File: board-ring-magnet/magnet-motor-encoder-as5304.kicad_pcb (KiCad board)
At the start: 2 copper layers, 38.7 x 12.7 mm, 11 parts, among them U1 DS18B20, U2 AS5304

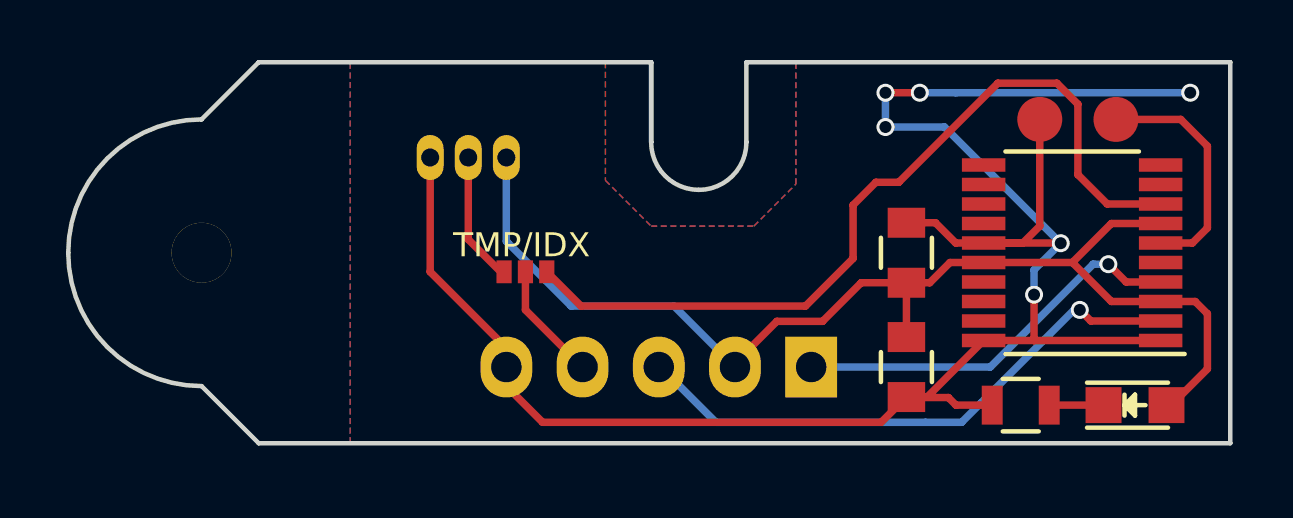
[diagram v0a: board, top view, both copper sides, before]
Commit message: board as5304: finish pcb layout and silkscreen
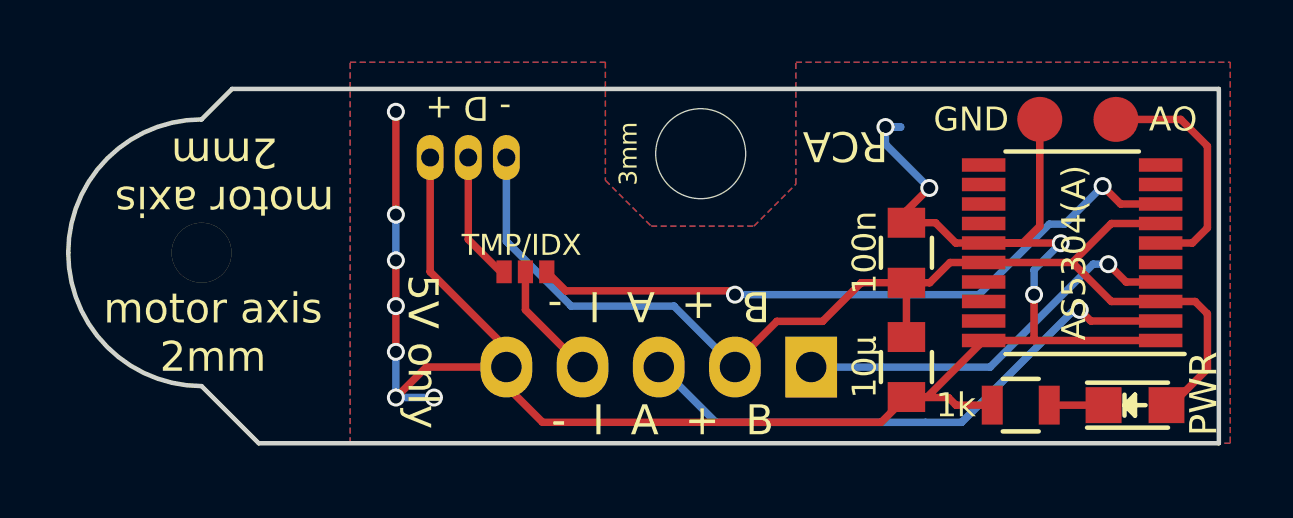
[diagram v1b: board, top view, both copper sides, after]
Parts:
- added REF**: 3mm, Mounting_Holes:MountingHole_3mm, F.Cu at (90.3, 43.7)
- U2: value AS5304 -> AS5304(A)
- renumbered GND to W1, AO to W2
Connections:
- net Net-(JP1-Pad1) renamed /B
- net Net-(JP1-Pad3) renamed /A
- net Net-(JP1-Pad4) renamed /TMP_IDX
- net Net-(SJ1-Pad1) renamed /TMP
- net Net-(SJ1-Pad3) renamed /IDX
- net Net-(U2-Pad6) renamed /AO
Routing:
- net /IDX: track 28.1 -> 22.5 mm, vias 0 -> 2
- net GND: track 68.5 -> 69.8 mm, vias 6 -> 11
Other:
- board size 38.7 x 12.7 mm -> 38.4 x 11.8 mm
- board text added: "- D +"
- board text added: "- I A + B"
- board text added: "2mm pole len. 44 pole ring magnet Ø in 24mm Ø out 32mm AS5000-MR20-44"
- board text added: "5V only"
- board text added: "B + A I -"
- board text added: "RCA"
- board text added: "magnet-motor- encoder AS5304(A) A. Wenzel R. Lehmann © RCA 2016"
- board text added: "motor axis 2mm"
